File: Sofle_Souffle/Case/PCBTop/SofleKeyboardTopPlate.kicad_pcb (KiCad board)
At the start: 2 copper layers, 143.4 x 111.8 mm, 9 parts

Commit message: Initial mod for the souffle top case.
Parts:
- added ?: , , F.Cu at (358.4, 82.1)
- added ?: , , F.Cu at (358.4, 84.8)
- added SW1: SW_PUSH-MX_W_LED, SofleRGB:SK6812MINI_and_cherry_NoLEDPads, F.Cu at (369.8, 53.0)
- added SW10: SW_PUSH-MX_W_LED, SofleRGB:SK6812MINI_and_cherry_NoLEDPads, F.Cu at (426.9, 69.6)
- added SW11: SW_PUSH-MX_W_LED, SofleRGB:SK6812MINI_and_cherry_NoLEDPads, F.Cu at (446.0, 74.4)
- added SW12: SW_PUSH-MX_W_LED, SofleRGB:SK6812MINI_and_cherry_NoLEDPads, F.Cu at (465.0, 74.4)
- added SW13: SW_PUSH-MX_W_LED, SofleRGB:SK6812MINI_and_cherry_NoLEDPads, F.Cu at (369.8, 91.1)
- added SW14: SW_PUSH-MX_W_LED, SofleRGB:SK6812MINI_and_cherry_NoLEDPads, F.Cu at (388.8, 88.6)
- added SW15: SW_PUSH-MX_W_LED, SofleRGB:SK6812MINI_and_cherry_NoLEDPads, F.Cu at (407.9, 86.0)
- added SW16: SW_PUSH-MX_W_LED, SofleRGB:SK6812MINI_and_cherry_NoLEDPads, F.Cu at (426.9, 88.7)
- added SW17: SW_PUSH-MX_W_LED, SofleRGB:SK6812MINI_and_cherry_NoLEDPads, F.Cu at (446.0, 93.5)
- added SW18: SW_PUSH-MX_W_LED, SofleRGB:SK6812MINI_and_cherry_NoLEDPads, F.Cu at (465.0, 93.5)
- added SW19: SW_PUSH-MX_W_LED, SofleRGB:SK6812MINI_and_cherry_NoLEDPads, F.Cu at (369.8, 110.1)
- added SW2: SW_PUSH-MX_W_LED, SofleRGB:SK6812MINI_and_cherry_NoLEDPads, F.Cu at (388.8, 50.5)
- added SW20: SW_PUSH-MX_W_LED, SofleRGB:SK6812MINI_and_cherry_NoLEDPads, F.Cu at (388.8, 107.6)
- added SW21: SW_PUSH-MX_W_LED, SofleRGB:SK6812MINI_and_cherry_NoLEDPads, F.Cu at (407.9, 105.1)
- added SW22: SW_PUSH-MX_W_LED, SofleRGB:SK6812MINI_and_cherry_NoLEDPads, F.Cu at (426.9, 107.7)
- added SW23: SW_PUSH-MX_W_LED, SofleRGB:SK6812MINI_and_cherry_NoLEDPads, F.Cu at (446.0, 112.5)
- added SW24: SW_PUSH-MX_W_LED, SofleRGB:SK6812MINI_and_cherry_NoLEDPads, F.Cu at (465.0, 112.5)
- added SW26: SW_PUSH-MX_W_LED, SofleRGB:SK6812MINI_and_cherry_NoLEDPads, F.Cu at (346.0, 136.4)
- added SW27: SW_PUSH-MX_W_LED, SofleRGB:SK6812MINI_and_cherry_NoLEDPads, F.Cu at (367.0, 131.3)
- added SW28: SW_PUSH-MX_W_LED, SofleRGB:SK6812MINI_and_cherry_NoLEDPads, F.Cu at (388.8, 126.7)
- added SW29: SW_PUSH-MX_W_LED, SofleRGB:SK6812MINI_and_cherry_NoLEDPads, F.Cu at (407.9, 124.1)
- added SW3: SW_PUSH-MX_W_LED, SofleRGB:SK6812MINI_and_cherry_NoLEDPads, F.Cu at (407.9, 47.9)
- added SW30: SW_PUSH-MX_W_LED, SofleRGB:SK6812MINI_and_cherry_NoLEDPads, F.Cu at (465.0, 131.6)
- added SW4: SW_PUSH-MX_W_LED, SofleRGB:SK6812MINI_and_cherry_NoLEDPads, F.Cu at (426.9, 50.6)
- added SW5: SW_PUSH-MX_W_LED, SofleRGB:SK6812MINI_and_cherry_NoLEDPads, F.Cu at (446.0, 55.4)
- added SW6: SW_PUSH-MX_W_LED, SofleRGB:SK6812MINI_and_cherry_NoLEDPads, F.Cu at (465.0, 55.4)
- added SW7: SW_PUSH-MX_W_LED, SofleRGB:SK6812MINI_and_cherry_NoLEDPads, F.Cu at (369.8, 72.0)
- added SW8: SW_PUSH-MX_W_LED, SofleRGB:SK6812MINI_and_cherry_NoLEDPads, F.Cu at (388.8, 69.5)
- added SW9: SW_PUSH-MX_W_LED, SofleRGB:SK6812MINI_and_cherry_NoLEDPads, F.Cu at (407.9, 67.0)
- added TH1: HOLE, SofleRGB:M2_HOLE_PCB, F.Cu at (356.3, 95.5)
- added TH2: HOLE, SofleRGB:M2_HOLE_PCB, F.Cu at (340.8, 95.5)
- added TH3: HOLE, SofleRGB:HOLE_M2_TH, F.Cu at (455.3, 102.7)
- added TH4: HOLE, SofleRGB:HOLE_M2_TH, F.Cu at (352.3, 121.7)
- added TH5: HOLE, SofleRGB:HOLE_M2_TH, F.Cu at (455.3, 64.6)
- added TH6: HOLE, SofleRGB:HOLE_M2_TH, F.Cu at (379.1, 99.9)
- added TH7: HOLE, SofleRGB:HOLE_M2_TH, F.Cu at (379.1, 59.8)
- added TH8: HOLE, SofleRGB:M2_HOLE_PCB, F.Cu at (351.8, 95.5)
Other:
- board size 143.4 x 111.8 mm -> 391.7 x 113.2 mm

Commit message: Moved SW30 to the pinky bottom.
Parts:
- removed ? (x2): , 
- removed SW1, SW10, SW11, SW12, SW13, SW14, SW15, SW16, SW17, SW18, SW19, SW2, SW20, SW21, SW22, SW23, SW24, SW26, SW27, SW28, SW29, SW3, SW30, SW4, SW5, SW6, SW7, SW8, SW9: SW_PUSH-MX_W_LED, SofleRGB:SK6812MINI_and_cherry_NoLEDPads
- removed TH1, TH2, TH8: HOLE, SofleRGB:M2_HOLE_PCB
- removed the TH3 at (455.3, 102.7)
- removed the TH4 at (352.3, 121.7)
- removed the TH5 at (455.3, 64.6)
- removed the TH6 at (379.1, 99.9)
- removed the TH7 at (379.1, 59.8)
- moved G*** 32.8 mm to (160.8, 132.4)
- moved G*** 32.8 mm to (160.1, 132.4)
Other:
- board size 391.7 x 113.2 mm -> 143.3 x 111.8 mm
- board text removed: "Sofle RGB v1.1, Dane Evans"

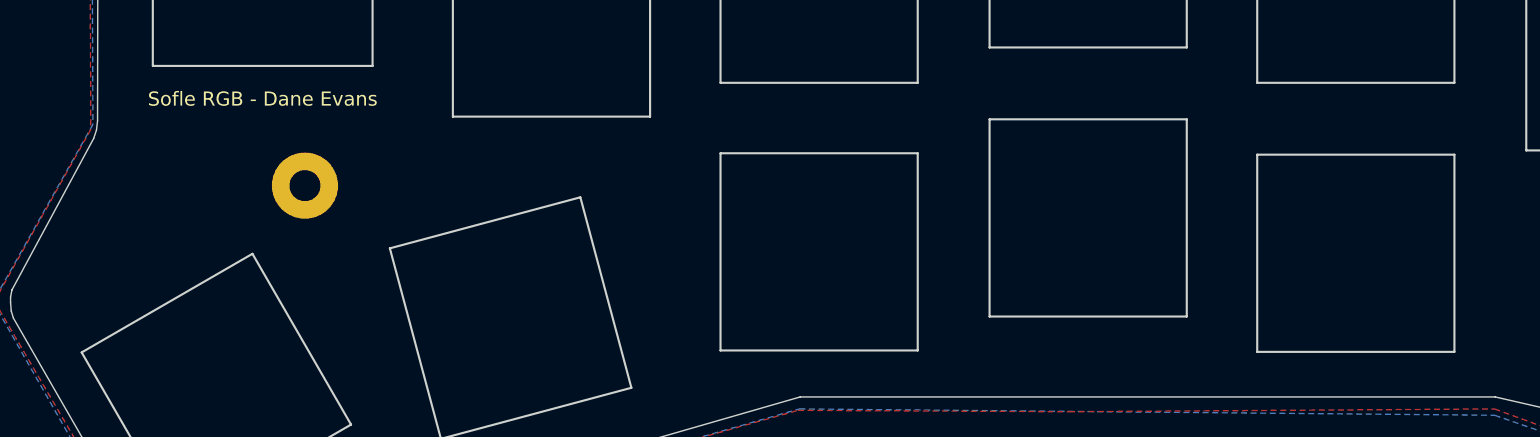
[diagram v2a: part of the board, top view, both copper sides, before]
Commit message: Removed 5pin connector on the right side of the case/pcb.
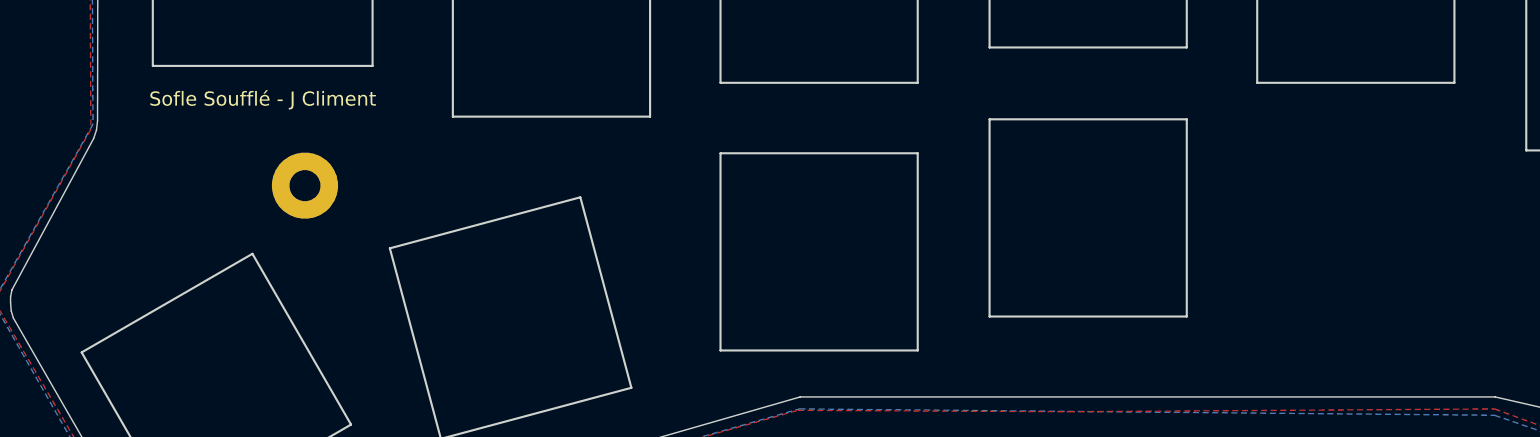
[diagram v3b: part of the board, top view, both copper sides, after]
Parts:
- moved G*** 39.3 mm to (200.1, 133.1)
- moved G*** 39.3 mm to (199.4, 133.1)
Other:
- outline, holes or cut-outs redrawn
- board text added: "Sofle Soufflé - J Climent"
- board text removed: "Sofle RGB - Dane Evans"
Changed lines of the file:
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@@
   (general
     (thickness 1.6)
-    (drawings 170)
+    (drawings 166)
     (tracks 0)
     (zones 0)
@@
   )
   (module dane:gecko-logo (layer B.Cu)
-    (at 160.806 132.438 180)
+    (at 200.143 133.128 180)
     (fp_text reference G*** (at 0 0) (layer B.SilkS) hide
       (effects (font (size 1.524 1.524) (thickness 0.3)) (justify mirror))
@@
   )
   (module dane:gecko-logo (layer F.Cu)
-    (at 160.056 132.438)
+    (at 199.393 133.128)
     (fp_text reference G*** (at 0 0) (layer F.SilkS) hide
       (effects (font (size 1.524 1.524) (thickness 0.3)))
@@
   (gr_arc (start 225.87082 139.13586) (end 225.865741 139.704819) (angle -90.5) (layer Edge.Cuts) (width 0.1))
   (gr_line (start 225.865741 139.704819) (end 207.1053 139.70482) (layer Edge.Cuts) (width 0.1))
-  (gr_text "Sofle RGB - Dane Evans\n" (at 101.495 114.3) (layer B.SilkS)
+  (gr_text "Sofle Soufflé - J Climent" (at 101.054 114.281) (layer B.SilkS)
     (effects (font (size 1 1) (thickness 0.2)) (justify mirror))
   )
-  (gr_text "Sofle RGB - Dane Evans\n" (at 100.995 114.3) (layer F.SilkS)
+  (gr_text "Sofle Soufflé - J Climent" (at 100.995 114.3) (layer F.SilkS)
     (effects (font (size 1 1) (thickness 0.2)))
   )
@@
   (gr_line (start 204.695 60.845) (end 190.695 60.845) (layer Edge.Cuts) (width 0.15))
   (gr_line (start 190.695 60.845) (end 190.695 46.845) (layer Edge.Cuts) (width 0.15))
-  (gr_line (start 185.595 118.245) (end 185.595 132.245) (layer Edge.Cuts) (width 0.15))
-  (gr_line (start 171.595 118.245) (end 185.595 118.245) (layer Edge.Cuts) (width 0.15))
-  (gr_line (start 185.595 132.245) (end 171.595 132.245) (layer Edge.Cuts) (width 0.15))
-  (gr_line (start 171.595 132.245) (end 171.595 118.245) (layer Edge.Cuts) (width 0.15))
   (gr_line (start 185.595 99.145) (end 185.595 113.145) (layer Edge.Cuts) (width 0.15))
   (gr_line (start 171.595 99.145) (end 185.595 99.145) (layer Edge.Cuts) (width 0.15))

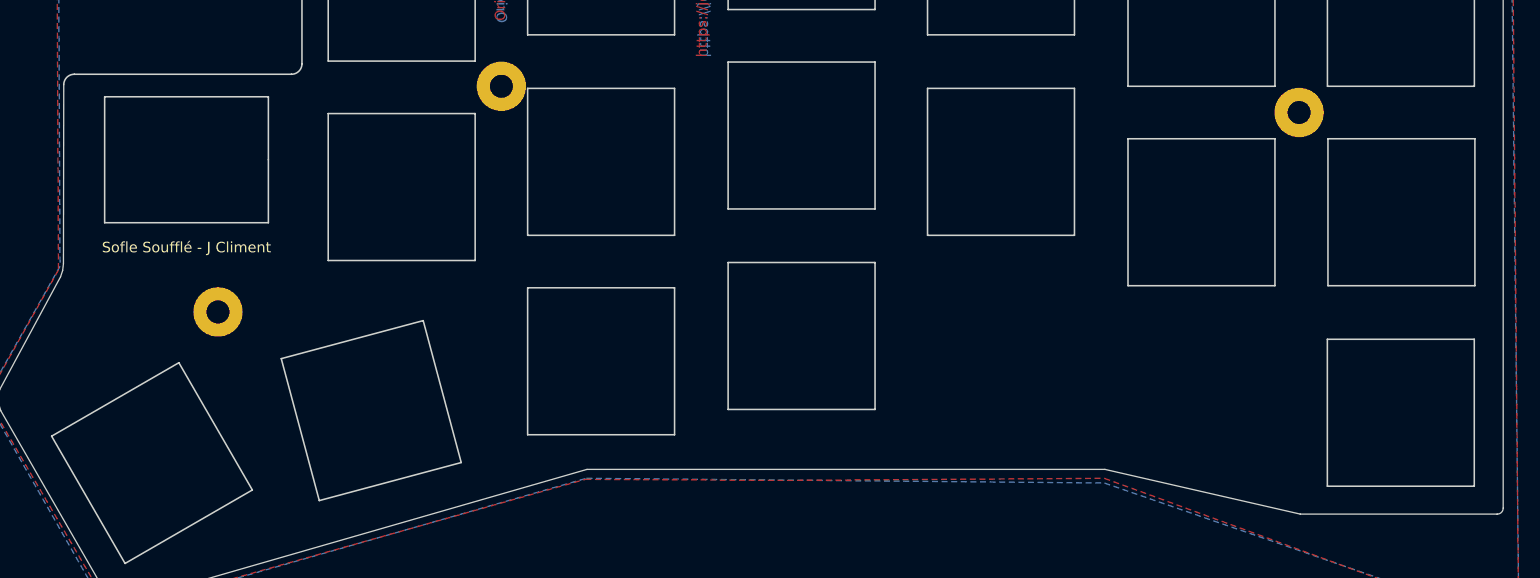
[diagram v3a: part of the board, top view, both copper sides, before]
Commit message: Corrected bottom plate.
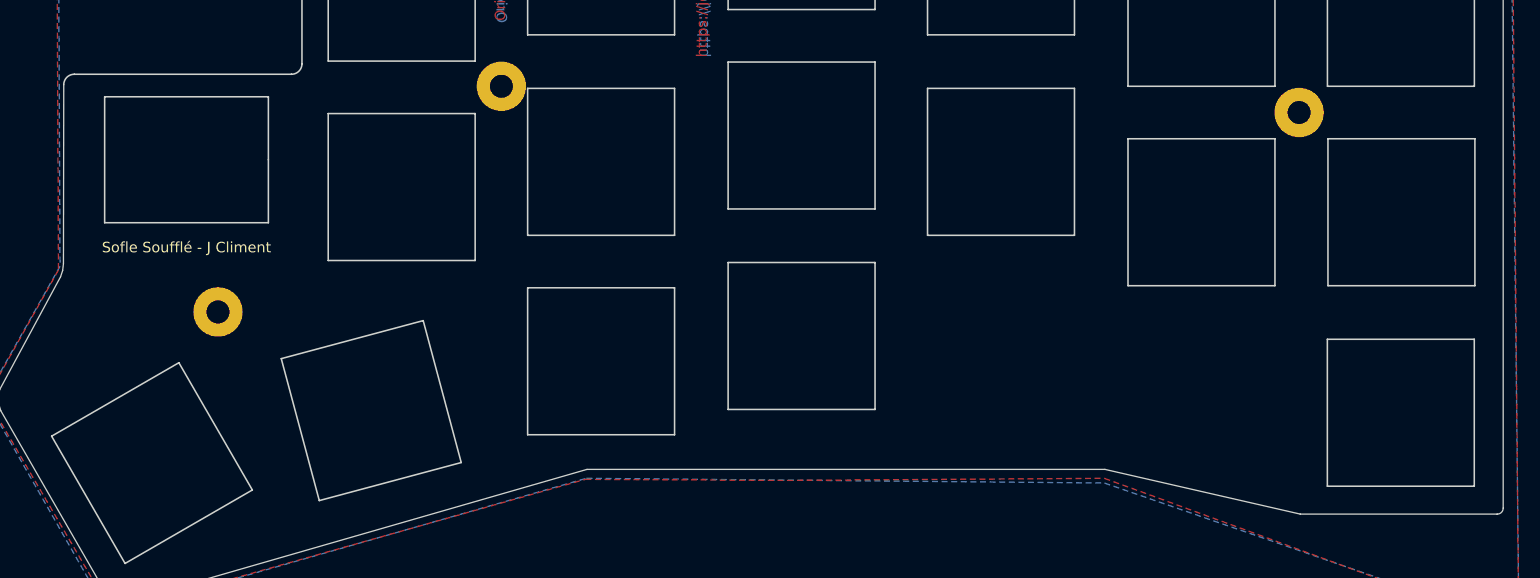
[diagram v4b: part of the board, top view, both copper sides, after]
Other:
- net class Default removed

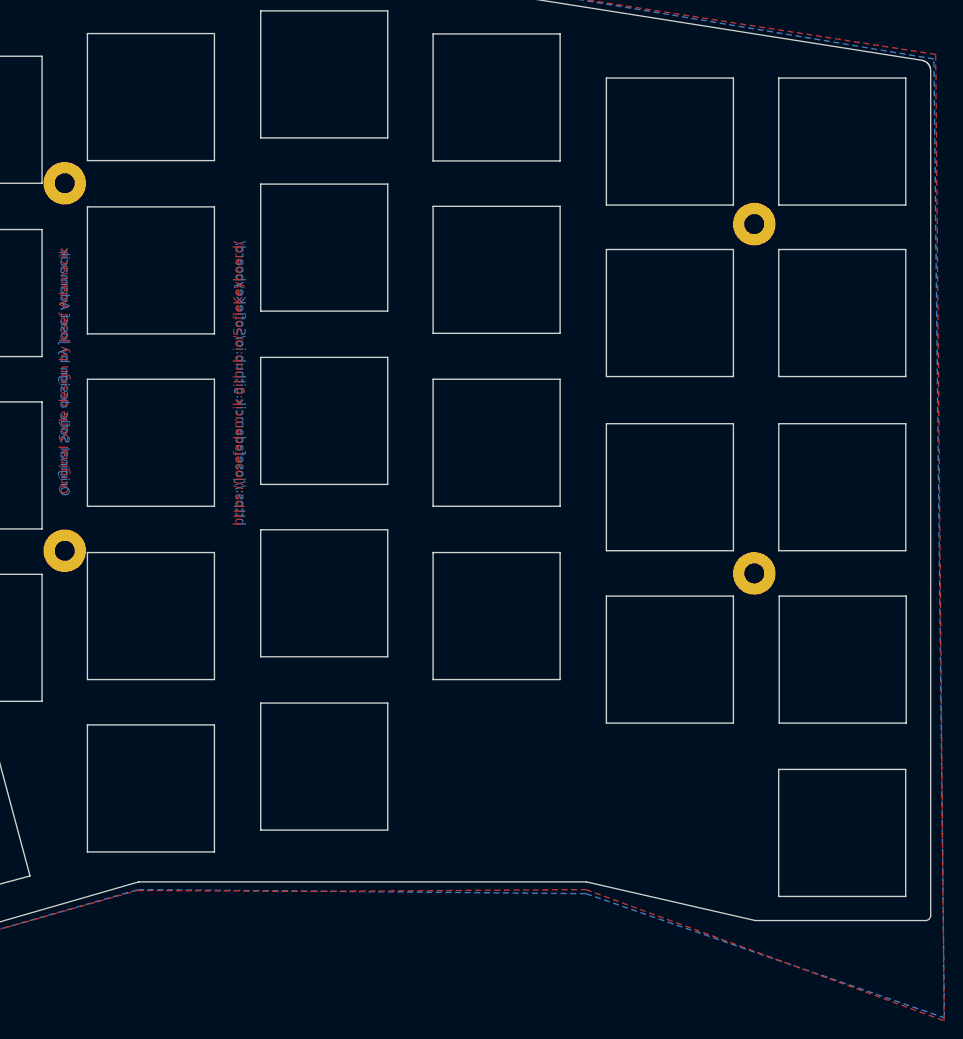
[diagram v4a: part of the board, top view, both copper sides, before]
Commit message: Fixed top case hole.
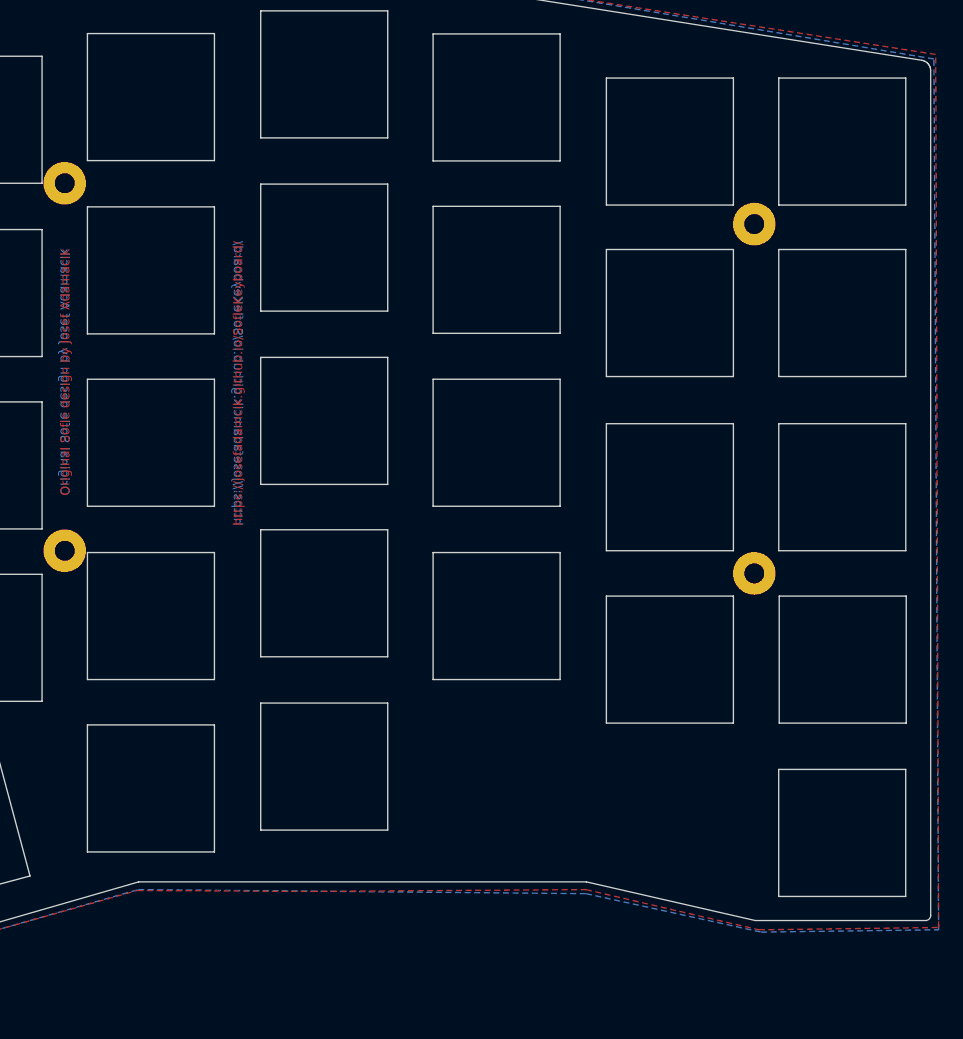
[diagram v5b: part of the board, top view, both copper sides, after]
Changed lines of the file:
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@@
     (effects (font (size 1 1) (thickness 0.15)))
   )
-  (gr_text "Original Sofle design by Josef Adamacik" (at 130.895 79.1 90) (layer "F.Cu")
-    (effects (font (size 1 1) (thickness 0.2)))
+  (gr_text "Original Sofle design by Josef Adamacik" (at 131.045 79.258 90) (layer "F.Cu")
+    (effects (font (size 1 1) (thickness 0.15)))
   )
-  (gr_text "https://josefadamcik.github.io/SofleKeyboard/" (at 150.395 80.5 270) (layer "B.Cu")
+  (gr_text "https://josefadamcik.github.io/SofleKeyboard/" (at 150.095 80.5 270) (layer "B.Cu")
     (effects (font (size 1 1) (thickness 0.15)) (justify mirror))
   )
-  (gr_text "Original Sofle design by Josef Adamacik" (at 130.995 79.3 270) (layer "B.Cu")
-    (effects (font (size 1 1) (thickness 0.2)) (justify mirror))
+  (gr_text "Original Sofle design by Josef Adamacik" (at 130.995 79.258 270) (layer "B.Cu")
+    (effects (font (size 1 1) (thickness 0.15)) (justify mirror))
   )
   (gr_text "Sofle Soufflé - J Climent" (at 101.054 114.281) (layer "B.SilkS")
@@
     (connect_pads (clearance 0.508))
     (min_thickness 0.254) (filled_areas_thickness no)
-    (fill yes (thermal_gap 0.508) (thermal_bridge_width 0.508))
+    (fill (thermal_gap 0.508) (thermal_bridge_width 0.508))
     (polygon
       (pts
@@
         (xy 158.245 136.495)
         (xy 188.445 136.295)
-        (xy 227.92 150.756)
+        (xy 207.499 140.726)
+        (xy 227.311 140.472)
         (xy 226.995 44.245)
         (xy 172.695 35.745)
@@
     (connect_pads (clearance 0.508))
     (min_thickness 0.254) (filled_areas_thickness no)
-    (fill yes (thermal_gap 0.508) (thermal_bridge_width 0.508))
+    (fill (thermal_gap 0.508) (thermal_bridge_width 0.508))
     (polygon
       (pts
@@
         (xy 139.095 136.295)
         (xy 188.445 136.745)
-        (xy 227.947 150.43)
+        (xy 207.753 140.98)
+        (xy 227.311 140.726)
         (xy 226.795 44.745)
         (xy 172.495 35.645)

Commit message: Case updates.
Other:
- outline, holes or cut-outs redrawn
